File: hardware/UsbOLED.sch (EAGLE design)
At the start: 23 parts, among them U1 ATMEGA328P-MU-QFN32, X1 USBPCB

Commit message: urther refine
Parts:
- removed JP1: (no value), adafruit:PINHD-1X6
- added H1: 1X6, headers(.1in):1X6
- R1: value 560kΩ -> 330kΩ
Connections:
- removed net N$10: C6.2, LCD1.VBAT
- net +3V3: now also C6.2, H1.5, LCD1.VBAT; no longer JP1.5
- net GND: now also H1.6; no longer JP1.6
- net MISO: now also H1.2; no longer JP1.2
- net MOSI: now also H1.1; no longer JP1.1
- net RST: now also H1.4; no longer JP1.4
- net SCK: now also H1.3; no longer JP1.3
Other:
- note added: "TODO : Why 5V and not 3V3?"
- note removed: "Investigate if 3.3 VReg still needed, since the OLED already has one."
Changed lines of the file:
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@@
 <setting verticaltext="up"/>
 </settings>
-<grid distance="0.1" unitdist="inch" unit="inch" style="lines" multiple="1" display="no" altdistance="0.01" altunitdist="inch" altunit="inch"/>
+<grid distance="0.05" unitdist="inch" unit="inch" style="lines" multiple="1" display="no" altdistance="0.01" altunitdist="inch" altunit="inch"/>
 <layers>
 <layer number="1" name="Top" color="4" fill="1" visible="no" active="no"/>
@@
 <part name="R7" library="SparkFun" deviceset="RESISTOR-ARRAY" device="0603-ARV" value="4.7kΩ"/>
 <part name="+3V8" library="supply1" deviceset="+3V3" device=""/>
-<part name="JP1" library="adafruit" deviceset="PINHD-1X6" device=""/>
 <part name="+3V6" library="supply1" deviceset="+3V3" device=""/>
 <part name="SUPPLY2" library="supply2" deviceset="GND" device=""/>
@@
 <part name="C2" library="rcl" deviceset="C-EU" device="C0603" value="1uF"/>
 <part name="C3" library="rcl" deviceset="C-EU" device="C0603" value="1uF"/>
-<part name="R1" library="rcl" deviceset="R-EU_" device="R0603" value="560kΩ"/>
+<part name="R1" library="rcl" deviceset="R-EU_" device="R0603" value="330kΩ"/>
 <part name="SUPPLY1" library="supply2" deviceset="GND" device=""/>
 <part name="C4" library="rcl" deviceset="C-EU" device="C0603" value="10uF"/>
@@
 <part name="D3" library="diode" deviceset="DIODE-" device="SOD523"/>
 <part name="P+1" library="supply1" deviceset="+5V" device=""/>
+<part name="+3V1" library="supply1" deviceset="+3V3" device=""/>
+<part name="H1" library="headers(.1in)" deviceset="1X6" device=""/>
 </parts>
 <sheets>
@@
 <wire x1="33.02" y1="320.04" x2="33.02" y2="238.76" width="0.1524" layer="95" style="longdash"/>
 <text x="-17.78" y="236.22" size="3.81" layer="95">MCU</text>
-<text x="10.16" y="104.14" size="1.27" layer="91">Investigate if 3.3 VReg still needed, since the OLED already has one.</text>
 <text x="25.4" y="114.3" size="1.27" layer="91">Source : https://wiki.52pi.com/index.php/0.91_OLED_(English)</text>
+<text x="-48.26" y="147.32" size="1.778" layer="91">TODO : Why 5V and not 3V3?</text>
 </plain>
 <instances>
@@
 <instance part="R7" gate="D" x="7.62" y="198.12"/>
 <instance part="+3V8" gate="G$1" x="30.48" y="220.98"/>
-<instance part="JP1" gate="A" x="-7.62" y="341.63"/>
 <instance part="+3V6" gate="G$1" x="-27.94" y="339.09" rot="R90"/>
 <instance part="SUPPLY2" gate="GND" x="-19.05" y="334.01"/>
@@
 <instance part="D3" gate="G$1" x="-20.32" y="134.62" rot="R180"/>
 <instance part="P+1" gate="1" x="-22.86" y="142.24"/>
+<instance part="+3V1" gate="G$1" x="2.54" y="152.4"/>
+<instance part="H1" gate="G$1" x="-13.97" y="341.63"/>
 </instances>
 <busses>
@@
 </segment>
 <segment>
-<pinref part="JP1" gate="A" pin="6"/>
-<wire x1="-10.16" y1="336.55" x2="-19.05" y2="336.55" width="0.1524" layer="91"/>
+<wire x1="-10.16" y1="336.55" x2="-11.43" y2="336.55" width="0.1524" layer="91"/>
 <pinref part="SUPPLY2" gate="GND" pin="GND"/>
+<pinref part="H1" gate="G$1" pin="6"/>
+<wire x1="-11.43" y1="336.55" x2="-19.05" y2="336.55" width="0.1524" layer="91"/>
+<junction x="-11.43" y="336.55"/>
 </segment>
 <segment>
@@
 </segment>
 <segment>
-<pinref part="JP1" gate="A" pin="4"/>
-<wire x1="-10.16" y1="341.63" x2="-19.05" y2="341.63" width="0.1524" layer="91"/>
+<wire x1="-10.16" y1="341.63" x2="-11.43" y2="341.63" width="0.1524" layer="91"/>
 <label x="-19.05" y="341.63" size="1.27" layer="95" rot="R180" xref="yes"/>
+<pinref part="H1" gate="G$1" pin="4"/>
+<wire x1="-11.43" y1="341.63" x2="-19.05" y2="341.63" width="0.1524" layer="91"/>
+<junction x="-11.43" y="341.63"/>
 </segment>
 </net>
@@
 </segment>
 <segment>
-<pinref part="JP1" gate="A" pin="5"/>
-<wire x1="-10.16" y1="339.09" x2="-25.4" y2="339.09" width="0.1524" layer="91"/>
+<wire x1="-10.16" y1="339.09" x2="-11.43" y2="339.09" width="0.1524" layer="91"/>
 <pinref part="+3V6" gate="G$1" pin="+3V3"/>
+<pinref part="H1" gate="G$1" pin="5"/>
+<wire x1="-11.43" y1="339.09" x2="-25.4" y2="339.09" width="0.1524" layer="91"/>
+<junction x="-11.43" y="339.09"/>
 </segment>
 <segment>
@@
 <pinref part="+3V16" gate="G$1" pin="+3V3"/>
 </segment>
+<segment>
+<pinref part="LCD1" gate="G$1" pin="VBAT"/>
+<wire x1="20.32" y1="144.78" x2="2.54" y2="144.78" width="0.1524" layer="91"/>
+<pinref part="C6" gate="G$1" pin="2"/>
+<pinref part="+3V1" gate="G$1" pin="+3V3"/>
+<wire x1="2.54" y1="149.86" x2="2.54" y2="144.78" width="0.1524" layer="91"/>
+<junction x="2.54" y="144.78"/>
+</segment>
 </net>
 <net name="ADCENA" class="0">
@@
 </segment>
 <segment>
-<pinref part="JP1" gate="A" pin="1"/>
-<wire x1="-10.16" y1="349.25" x2="-19.05" y2="349.25" width="0.1524" layer="91"/>
+<wire x1="-10.16" y1="349.25" x2="-11.43" y2="349.25" width="0.1524" layer="91"/>
 <label x="-19.05" y="349.25" size="1.27" layer="95" rot="R180" xref="yes"/>
+<pinref part="H1" gate="G$1" pin="1"/>
+<wire x1="-11.43" y1="349.25" x2="-19.05" y2="349.25" width="0.1524" layer="91"/>
+<junction x="-11.43" y="349.25"/>
 </segment>
 </net>
@@
 </segment>
 <segment>
-<pinref part="JP1" gate="A" pin="2"/>
-<wire x1="-10.16" y1="346.71" x2="-19.05" y2="346.71" width="0.1524" layer="91"/>
+<wire x1="-10.16" y1="346.71" x2="-11.43" y2="346.71" width="0.1524" layer="91"/>
 <label x="-19.05" y="346.71" size="1.27" layer="95" rot="R180" xref="yes"/>
+<pinref part="H1" gate="G$1" pin="2"/>
+<wire x1="-11.43" y1="346.71" x2="-19.05" y2="346.71" width="0.1524" layer="91"/>
+<junction x="-11.43" y="346.71"/>
 </segment>
 </net>
@@
 </segment>
 <segment>
-<pinref part="JP1" gate="A" pin="3"/>
-<wire x1="-10.16" y1="344.17" x2="-19.05" y2="344.17" width="0.1524" layer="91"/>
+<wire x1="-10.16" y1="344.17" x2="-11.43" y2="344.17" width="0.1524" layer="91"/>
 <label x="-19.05" y="344.17" size="1.27" layer="95" rot="R180" xref="yes"/>
+<pinref part="H1" gate="G$1" pin="3"/>
+<wire x1="-11.43" y1="344.17" x2="-19.05" y2="344.17" width="0.1524" layer="91"/>
+<junction x="-11.43" y="344.17"/>
 </segment>
 </net>
@@
 </segment>
 </net>
-<net name="N$10" class="0">
-<segment>
-<pinref part="LCD1" gate="G$1" pin="VBAT"/>
-<wire x1="20.32" y1="144.78" x2="2.54" y2="144.78" width="0.1524" layer="91"/>
-<pinref part="C6" gate="G$1" pin="2"/>
-</segment>
-</net>

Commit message: Improve routing, add version
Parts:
- removed C4: 10uF, rcl:C-EUC0603
- removed C6, C7: 1uF, rcl:C-EUC0603
- removed D3: (no value), diode:DIODE-SOD523
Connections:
- removed net N$11: C4.2, LCD1.VCC
- removed net N$9: C7.2, LCD1.VDD
- net +3V3: now also LCD1.VDD; no longer C6.2
- net +5V: no longer D3.C
- net GND: no longer C4.1, C6.1, C7.1
- net OLED_RESET: no longer D3.A
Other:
- note removed: "TODO : Why 5V and not 3V3?"
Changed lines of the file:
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@@
 <part name="R1" library="rcl" deviceset="R-EU_" device="R0603" value="330kΩ"/>
 <part name="SUPPLY1" library="supply2" deviceset="GND" device=""/>
-<part name="C4" library="rcl" deviceset="C-EU" device="C0603" value="10uF"/>
 <part name="C5" library="rcl" deviceset="C-EU" device="C0603" value="10uF"/>
-<part name="C6" library="rcl" deviceset="C-EU" device="C0603" value="1uF"/>
-<part name="C7" library="rcl" deviceset="C-EU" device="C0603" value="1uF"/>
-<part name="D3" library="diode" deviceset="DIODE-" device="SOD523"/>
-<part name="P+1" library="supply1" deviceset="+5V" device=""/>
 <part name="+3V1" library="supply1" deviceset="+3V3" device=""/>
 <part name="H1" library="headers(.1in)" deviceset="1X6" device=""/>
@@
 <text x="-17.78" y="236.22" size="3.81" layer="95">MCU</text>
 <text x="25.4" y="114.3" size="1.27" layer="91">Source : https://wiki.52pi.com/index.php/0.91_OLED_(English)</text>
-<text x="-48.26" y="147.32" size="1.778" layer="91">TODO : Why 5V and not 3V3?</text>
 </plain>
 <instances>
@@
 <instance part="R1" gate="G$1" x="-2.54" y="127" rot="R180"/>
 <instance part="SUPPLY1" gate="GND" x="-7.62" y="111.76"/>
-<instance part="C4" gate="G$1" x="7.62" y="119.38" rot="R90"/>
 <instance part="C5" gate="G$1" x="7.62" y="124.46" rot="R90"/>
-<instance part="C6" gate="G$1" x="-2.54" y="144.78" rot="R90"/>
-<instance part="C7" gate="G$1" x="-2.54" y="137.16" rot="R90"/>
-<instance part="D3" gate="G$1" x="-20.32" y="134.62" rot="R180"/>
-<instance part="P+1" gate="1" x="-22.86" y="142.24"/>
 <instance part="+3V1" gate="G$1" x="2.54" y="152.4"/>
 <instance part="H1" gate="G$1" x="-13.97" y="341.63"/>
@@
 <pinref part="R1" gate="G$1" pin="2"/>
 <pinref part="SUPPLY1" gate="GND" pin="GND"/>
-<wire x1="-7.62" y1="114.3" x2="-7.62" y2="119.38" width="0.1524" layer="91"/>
-<pinref part="C4" gate="G$1" pin="1"/>
-<wire x1="-7.62" y1="119.38" x2="-7.62" y2="124.46" width="0.1524" layer="91"/>
+<wire x1="-7.62" y1="114.3" x2="-7.62" y2="124.46" width="0.1524" layer="91"/>
 <wire x1="-7.62" y1="124.46" x2="-7.62" y2="127" width="0.1524" layer="91"/>
-<wire x1="5.08" y1="119.38" x2="-7.62" y2="119.38" width="0.1524" layer="91"/>
-<junction x="-7.62" y="119.38"/>
 <pinref part="C5" gate="G$1" pin="1"/>
 <wire x1="5.08" y1="124.46" x2="-7.62" y2="124.46" width="0.1524" layer="91"/>
 <junction x="-7.62" y="124.46"/>
-<pinref part="C6" gate="G$1" pin="1"/>
-<wire x1="-5.08" y1="144.78" x2="-7.62" y2="144.78" width="0.1524" layer="91"/>
-<wire x1="-7.62" y1="144.78" x2="-7.62" y2="139.7" width="0.1524" layer="91"/>
 <junction x="-7.62" y="127"/>
 <pinref part="LCD1" gate="G$1" pin="VSS"/>
-<wire x1="-7.62" y1="139.7" x2="-7.62" y2="137.16" width="0.1524" layer="91"/>
-<wire x1="-7.62" y1="137.16" x2="-7.62" y2="127" width="0.1524" layer="91"/>
+<wire x1="-7.62" y1="139.7" x2="-7.62" y2="127" width="0.1524" layer="91"/>
 <wire x1="20.32" y1="139.7" x2="-7.62" y2="139.7" width="0.1524" layer="91"/>
-<junction x="-7.62" y="139.7"/>
-<pinref part="C7" gate="G$1" pin="1"/>
-<wire x1="-5.08" y1="137.16" x2="-7.62" y2="137.16" width="0.1524" layer="91"/>
-<junction x="-7.62" y="137.16"/>
 </segment>
 </net>
@@
 <pinref part="LCD1" gate="G$1" pin="VBAT"/>
 <wire x1="20.32" y1="144.78" x2="2.54" y2="144.78" width="0.1524" layer="91"/>
-<pinref part="C6" gate="G$1" pin="2"/>
 <pinref part="+3V1" gate="G$1" pin="+3V3"/>
 <wire x1="2.54" y1="149.86" x2="2.54" y2="144.78" width="0.1524" layer="91"/>
+<pinref part="LCD1" gate="G$1" pin="VDD"/>
+<wire x1="20.32" y1="137.16" x2="2.54" y2="137.16" width="0.1524" layer="91"/>
+<wire x1="2.54" y1="137.16" x2="2.54" y2="144.78" width="0.1524" layer="91"/>
 <junction x="2.54" y="144.78"/>
 </segment>
@@
 <pinref part="C9" gate="G$1" pin="1"/>
 <junction x="63.5" y="187.96"/>
-</segment>
-<segment>
-<pinref part="P+1" gate="1" pin="+5V"/>
-<pinref part="D3" gate="G$1" pin="C"/>
-<wire x1="-22.86" y1="139.7" x2="-22.86" y2="134.62" width="0.1524" layer="91"/>
 </segment>
 </net>
@@
 </segment>
 </net>
-<net name="N$9" class="0">
-<segment>
-<pinref part="LCD1" gate="G$1" pin="VDD"/>
-<wire x1="20.32" y1="137.16" x2="2.54" y2="137.16" width="0.1524" layer="91"/>
-<pinref part="C7" gate="G$1" pin="2"/>
-</segment>
-</net>
 <net name="N$7" class="0">
 <segment>
@@
 </segment>
 </net>
-<net name="N$11" class="0">
-<segment>
-<pinref part="LCD1" gate="G$1" pin="VCC"/>
-<pinref part="C4" gate="G$1" pin="2"/>
-<wire x1="20.32" y1="121.92" x2="20.32" y2="119.38" width="0.1524" layer="91"/>
-<wire x1="20.32" y1="119.38" x2="12.7" y2="119.38" width="0.1524" layer="91"/>
-</segment>
-</net>
 <net name="OLED_RESET" class="0">
 <segment>
@@
 <segment>
 <pinref part="LCD1" gate="G$1" pin="RES#"/>
-<label x="-15.24" y="134.62" size="1.27" layer="95" rot="R90" xref="yes"/>
-<pinref part="D3" gate="G$1" pin="A"/>
+<label x="-17.78" y="134.62" size="1.27" layer="95" rot="R90" xref="yes"/>
 <wire x1="20.32" y1="134.62" x2="-17.78" y2="134.62" width="0.1524" layer="91"/>
 </segment>
@@
 </sheet>
 </sheets>
+<errors>
+</errors>
 </schematic>
 </drawing>

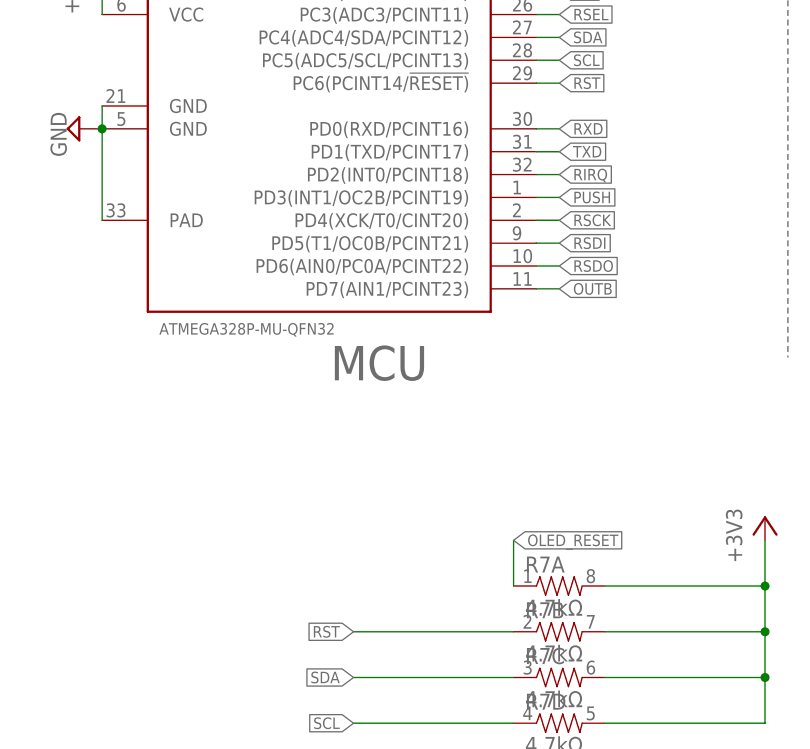
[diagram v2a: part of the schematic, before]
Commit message: Add pushbuttons A,B
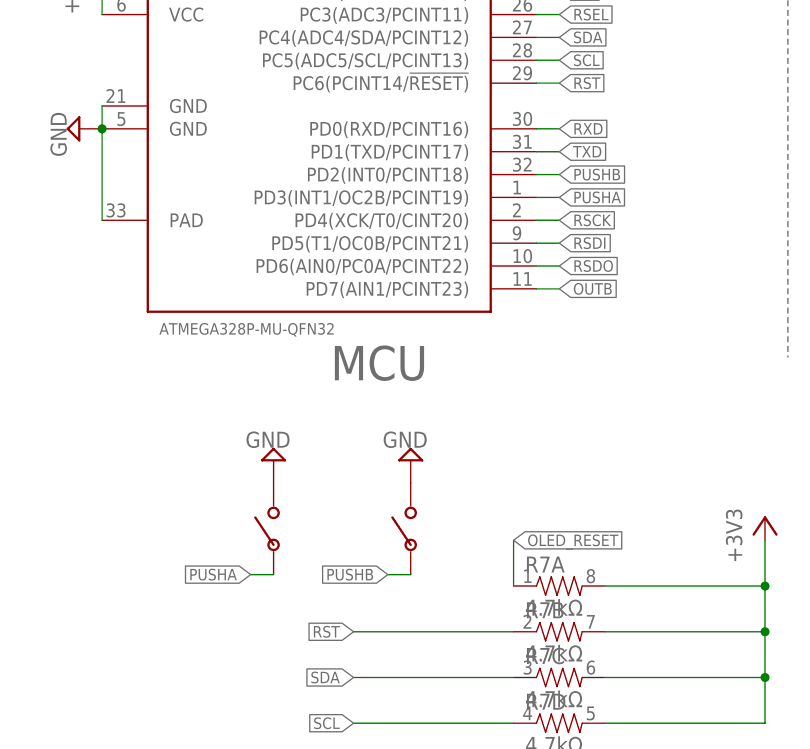
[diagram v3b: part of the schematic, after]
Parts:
- added U$1, U$3: PUSHBUTTON_4X2.5, pusbbutton_4x2_5:PUSHBUTTON_4X2.5
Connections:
- removed net PUSH: U1.PD3(INT1/OC2B/PCINT19)
- removed net RIRQ: U1.PD2(INT0/PCINT18)
- new net PUSHA: U$1.P$1, U1.PD3(INT1/OC2B/PCINT19)
- new net PUSHB: U$3.P$1, U1.PD2(INT0/PCINT18)
- net GND: now also U$1.P$2, U$3.P$2
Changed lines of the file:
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@@
 <part name="+3V1" library="supply1" deviceset="+3V3" device=""/>
 <part name="H1" library="headers(.1in)" deviceset="1X6" device=""/>
+<part name="SUPPLY32" library="supply2" deviceset="GND" device=""/>
+<part name="U$3" library="pusbbutton_4x2_5" deviceset="PUSHBUTTON_4X2.5" device=""/>
+<part name="SUPPLY5" library="supply2" deviceset="GND" device=""/>
+<part name="U$1" library="pusbbutton_4x2_5" deviceset="PUSHBUTTON_4X2.5" device=""/>
 </parts>
 <sheets>
@@
 <instance part="+3V1" gate="G$1" x="2.54" y="152.4"/>
 <instance part="H1" gate="G$1" x="-13.97" y="341.63"/>
+<instance part="SUPPLY32" gate="GND" x="-8.89" y="227.33" rot="R180"/>
+<instance part="U$3" gate="G$1" x="-8.89" y="219.71" rot="R90"/>
+<instance part="SUPPLY5" gate="GND" x="-24.13" y="227.33" rot="R180"/>
+<instance part="U$1" gate="G$1" x="-24.13" y="219.71" rot="R90"/>
 </instances>
 <busses>
@@
 <wire x1="20.32" y1="139.7" x2="-7.62" y2="139.7" width="0.1524" layer="91"/>
 </segment>
+<segment>
+<pinref part="U$3" gate="G$1" pin="P$2"/>
+<pinref part="SUPPLY32" gate="GND" pin="GND"/>
+</segment>
+<segment>
+<pinref part="U$1" gate="G$1" pin="P$2"/>
+<pinref part="SUPPLY5" gate="GND" pin="GND"/>
+</segment>
 </net>
 <net name="SDA" class="0">
@@
 <wire x1="5.08" y1="248.92" x2="7.62" y2="248.92" width="0.1524" layer="91"/>
 <label x="7.62" y="248.92" size="1.27" layer="95" xref="yes"/>
-</segment>
-</net>
-<net name="RIRQ" class="0">
-<segment>
-<pinref part="U1" gate="G$1" pin="PD2(INT0/PCINT18)"/>
-<wire x1="5.08" y1="259.08" x2="7.62" y2="259.08" width="0.1524" layer="91"/>
-<label x="7.62" y="259.08" size="1.27" layer="95" xref="yes"/>
 </segment>
 </net>
@@
 </segment>
 </net>
-<net name="PUSH" class="0">
-<segment>
-<pinref part="U1" gate="G$1" pin="PD3(INT1/OC2B/PCINT19)"/>
-<wire x1="5.08" y1="256.54" x2="7.62" y2="256.54" width="0.1524" layer="91"/>
-<label x="7.62" y="256.54" size="1.27" layer="95" xref="yes"/>
-</segment>
-</net>
 <net name="RXD" class="0">
 <segment>
@@
 </segment>
 </net>
+<net name="PUSHB" class="0">
+<segment>
+<pinref part="U1" gate="G$1" pin="PD2(INT0/PCINT18)"/>
+<wire x1="5.08" y1="259.08" x2="7.62" y2="259.08" width="0.1524" layer="91"/>
+<label x="7.62" y="259.08" size="1.27" layer="95" xref="yes"/>
+</segment>
+<segment>
+<pinref part="U$3" gate="G$1" pin="P$1"/>
+<wire x1="-8.89" y1="214.63" x2="-11.43" y2="214.63" width="0.1524" layer="91"/>
+<label x="-11.43" y="214.63" size="1.27" layer="95" rot="R180" xref="yes"/>
+</segment>
+</net>
+<net name="PUSHA" class="0">
+<segment>
+<pinref part="U1" gate="G$1" pin="PD3(INT1/OC2B/PCINT19)"/>
+<wire x1="5.08" y1="256.54" x2="7.62" y2="256.54" width="0.1524" layer="91"/>
+<label x="7.62" y="256.54" size="1.27" layer="95" xref="yes"/>
+</segment>
+<segment>
+<pinref part="U$1" gate="G$1" pin="P$1"/>
+<wire x1="-24.13" y1="214.63" x2="-26.67" y2="214.63" width="0.1524" layer="91"/>
+<label x="-26.67" y="214.63" size="1.27" layer="95" rot="R180" xref="yes"/>
+</segment>
+</net>
